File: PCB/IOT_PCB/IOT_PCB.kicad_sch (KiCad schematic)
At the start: 6 parts, among them J1 Screw_Terminal_01x02, J2 Screw_Terminal_01x02, U1 ESP32-S3-WROOM-1, U2 BME280, U3 SCD41-D-R2

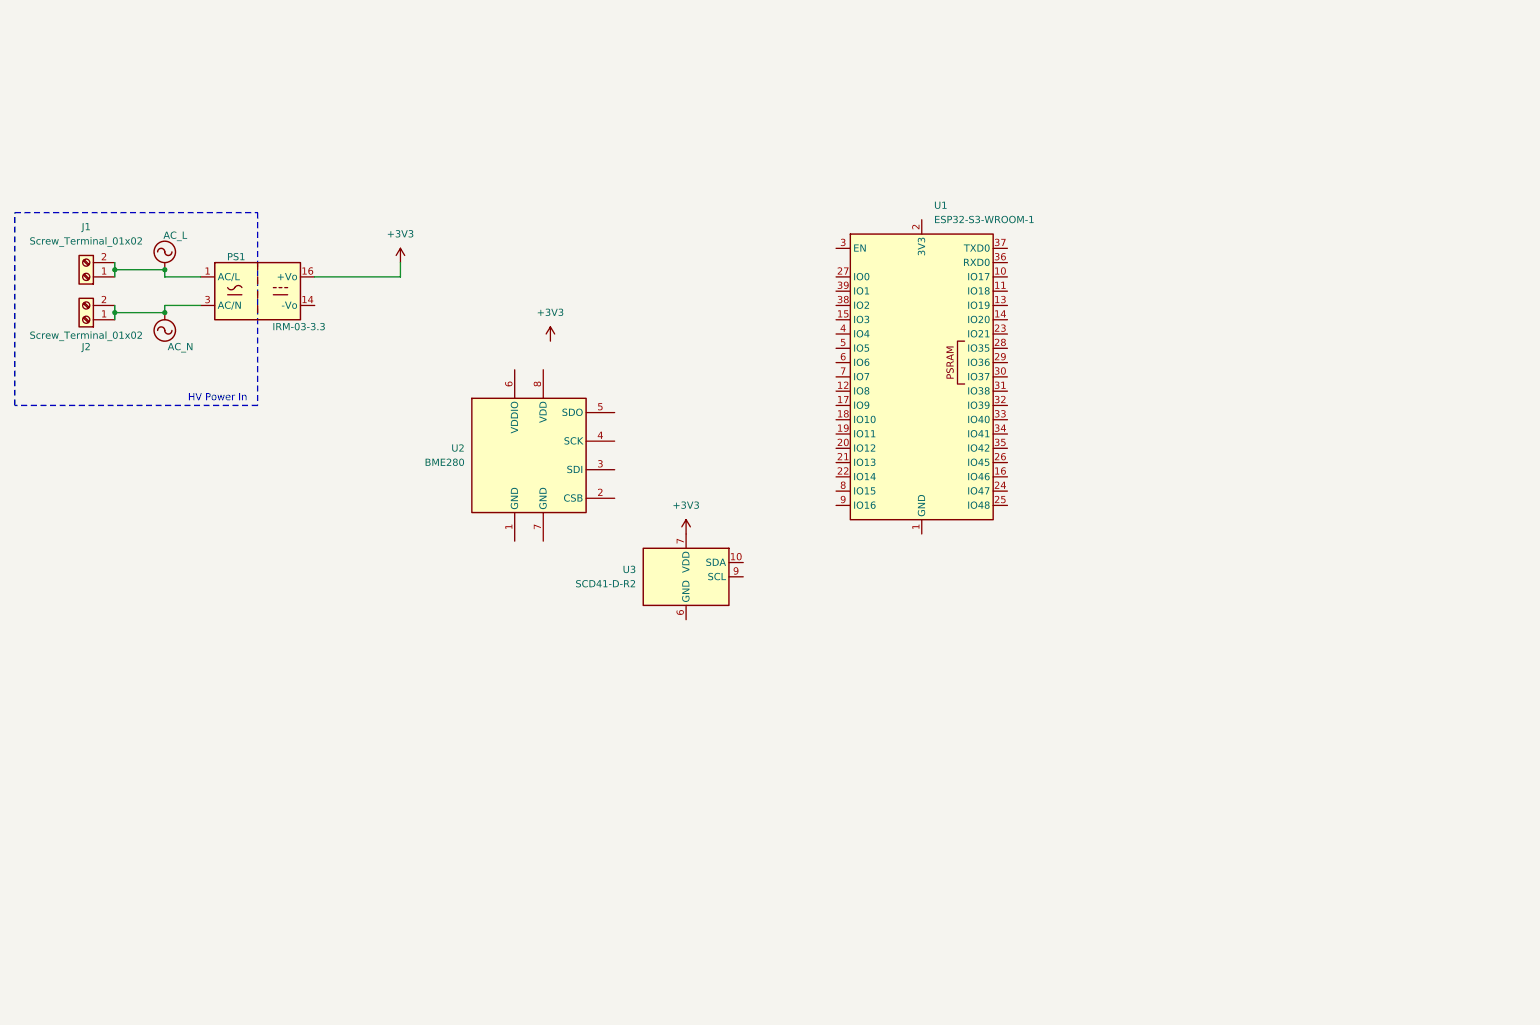
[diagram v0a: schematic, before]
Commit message: Rough component placement and schematic WIP
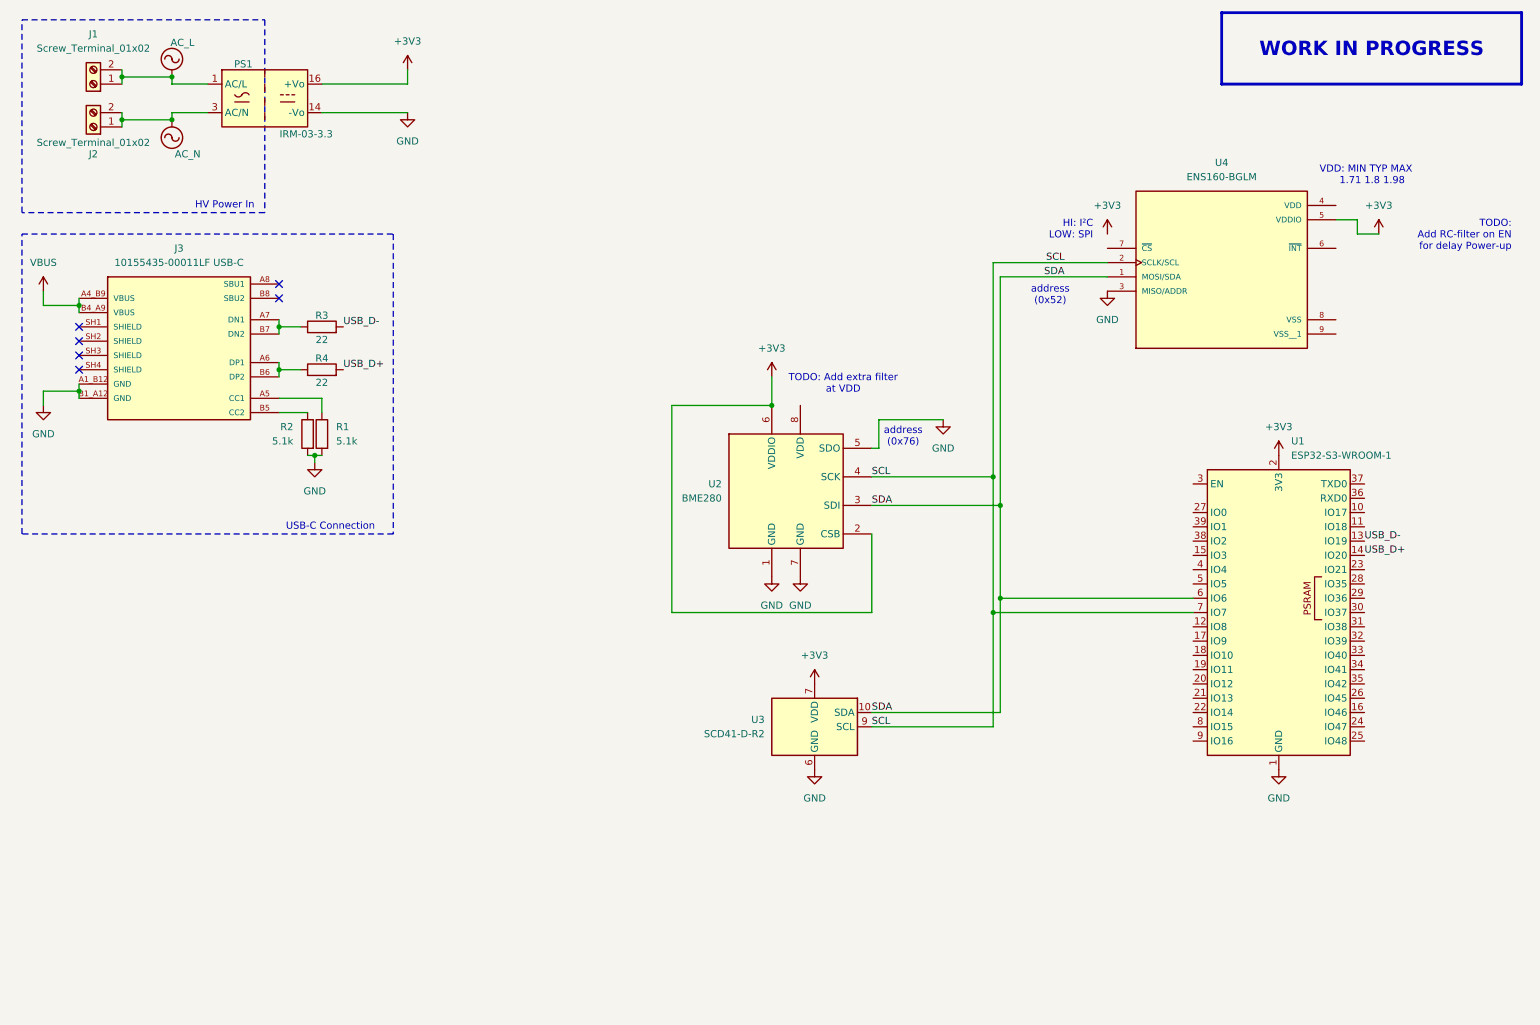
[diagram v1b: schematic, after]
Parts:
- added J3: 10155435-00011LF USB-C, USBC_2 Amphenol 10155435-00011LF:AMPHENOL_10155435-00011LF, symbol 10155435-00011LF:10155435-00011LF
- added R1, R2: 5.1k, Resistor_SMD:R_0805_2012Metric_Pad1.20x1.40mm_HandSolder, symbol Device:R
- added R3, R4: 22, Resistor_SMD:R_0805_2012Metric_Pad1.20x1.40mm_HandSolder, symbol Device:R
- added U4: ENS160-BGLM, ENS160_BGLM:XDCR_ENS160-BGLM, symbol ENS160-BGLM:ENS160-BGLM
- PS1: MANUFACTURER (none) -> Mean Well
- U1: Fält7 ESP32-S3-WROOM-1-N4 -> (none); MANUFACTURER (none) -> Espressif; Mouser No (none) -> 356-ESP32-S3WROOM1N4
- U2: MANUFACTURER (none) -> Bosch
- U3: MANUFACTURER (none) -> Sensirion
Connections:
- net +3V3: now also U1.2 (3V3), U2.2 (CSB), U2.6 (VDDIO), U4.5 (VDDIO)
- net SDA: now reaches U3.10 (SDA)
- net SDA: now also U1.6 (IO6), U2.3 (SDI), U4.1 (MOSI/SDA)
- net GND: now reaches U3.20 (GND), U3.21 (GND), U3.6 (GND)
- net GND: now also PS1.14 (-Vo), U1.1 (GND), U1.40 (GND), U1.41 (GND), U2.1 (GND), U2.5 (SDO), U2.7 (GND), J3.A1_B12 (GND), J3.B1_A12 (GND), R1.2, R2.2, U4.3 (MISO/ADDR)
- net SCL: now reaches U3.9 (SCL)
- net SCL: now also U1.7 (IO7), U2.4 (SCK), U4.2 (SCLK/SCL)
- net USB_D-: now reaches U1.13 (IO19)
- net USB_D-: now also R3.2
- net USB_D+: now reaches U1.14 (IO20)
- net USB_D+: now also R4.2
- new net: J3.A5 (CC1), R1.1
- new net: J3.A6 (DP1), J3.B6 (DP2), R4.1
- new net: J3.A7 (DN1), J3.B7 (DN2), R3.1
- new net: J3.B5 (CC2), R2.1
- new net VBUS: J3.A4_B9 (VBUS), J3.B4_A9 (VBUS)
- no-connect marks 0 -> 6
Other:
- note added: "HI: I²C LOW: SPI"
- note added: "TODO: Add RC-filter on EN for delay Power-up"
- note added: "TODO: Add extra filter at VDD"
- note added: "USB-C Connection"
- note added: "VDD: MIN TYP MAX 1.71 1.8 1.98"
- note added: "address (0x52)"
- note added: "address (0x76)"
- company: (none) -> By: Theofil Eriksson Petrovski
- title: (none) -> Environmental Sensing Module
- moved on the sheet: J1, J2, PS1, U1, U2, U3

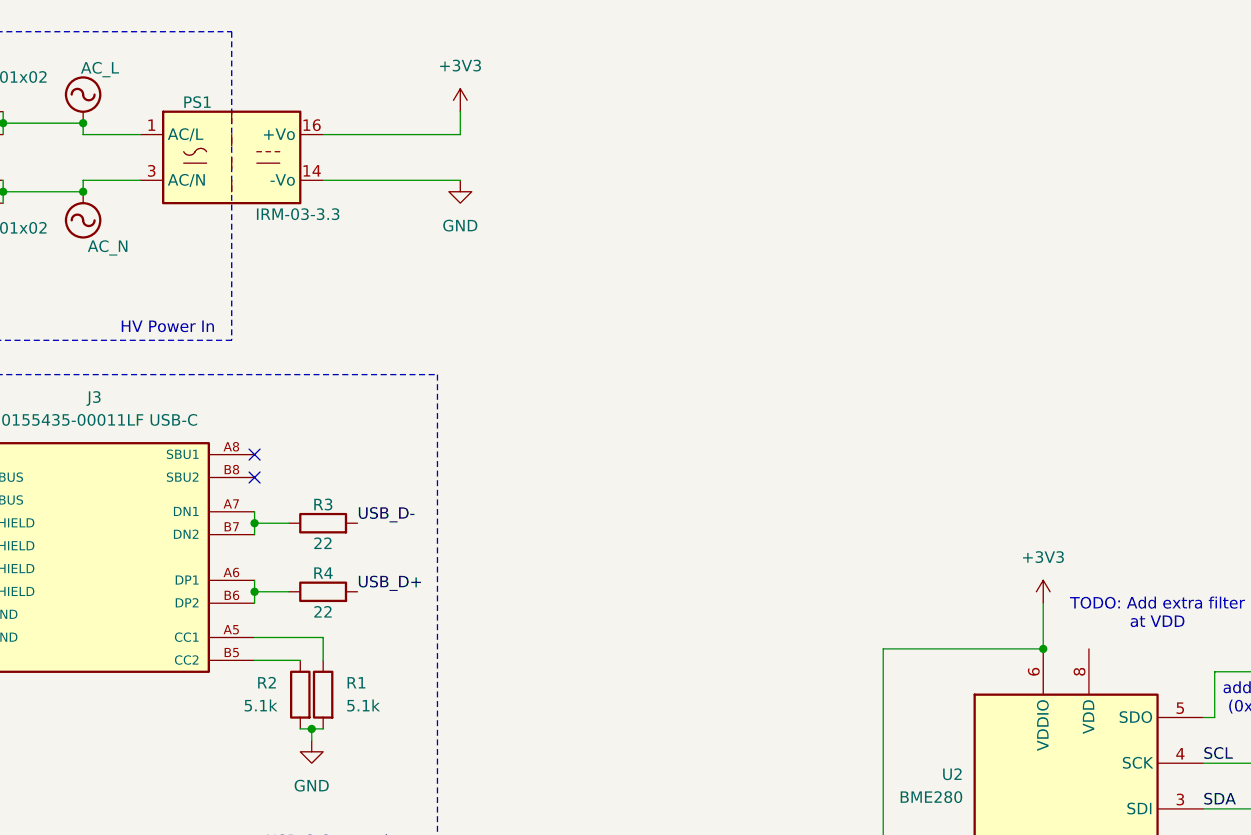
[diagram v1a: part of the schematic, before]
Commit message: Vreg and ESD suppresion
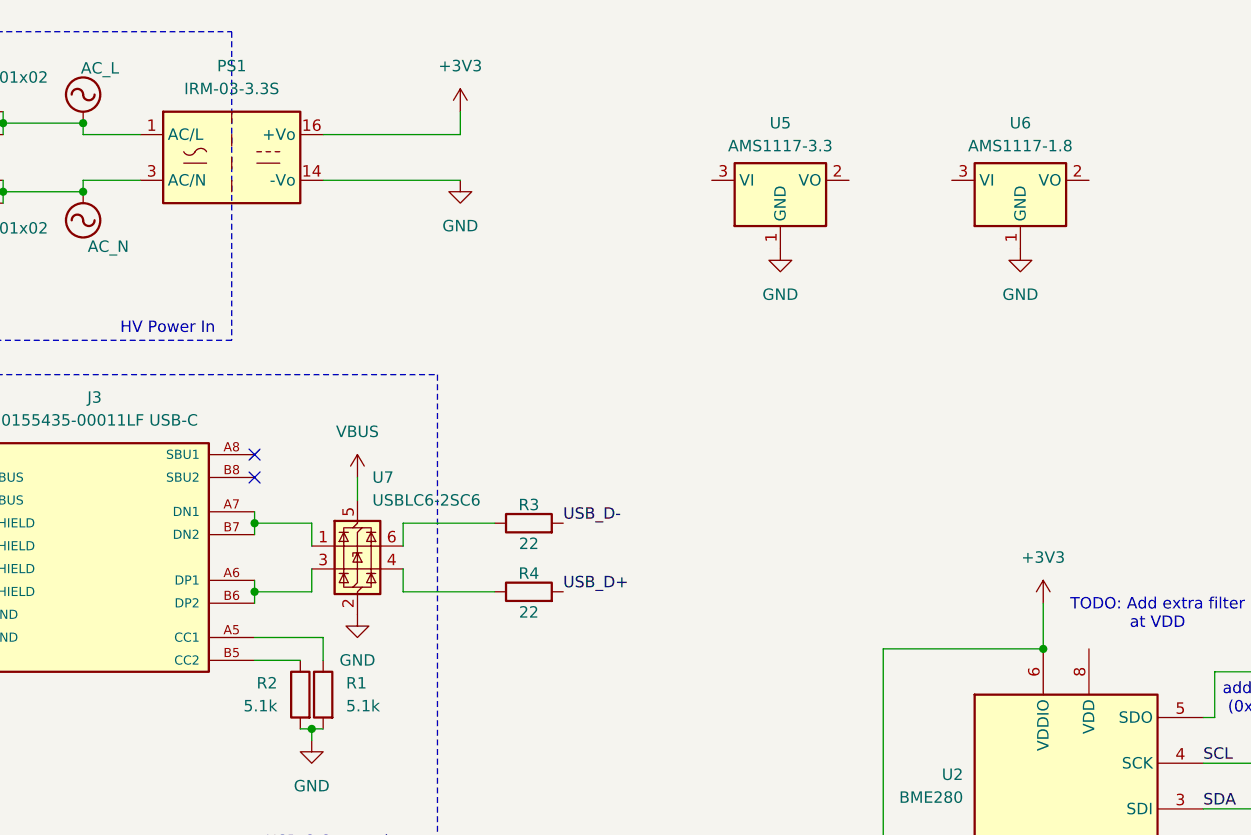
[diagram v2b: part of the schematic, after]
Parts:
- removed PS1: IRM-03-3.3, Converter_ACDC:Converter_ACDC_MeanWell_IRM-03-xx_THT, symbol Converter_ACDC:IRM-03-3.3
- added PS1: IRM-03-3.3S, Converter_ACDC:Converter_ACDC_MeanWell_IRM-03-xx_SMD, symbol Converter_ACDC:IRM-03-3.3S
- added U5: AMS1117-3.3, Package_TO_SOT_SMD:SOT-223-3_TabPin2, symbol Regulator_Linear:AMS1117-3.3
- added U6: AMS1117-1.8, Package_TO_SOT_SMD:SOT-223-3_TabPin2, symbol Regulator_Linear:AMS1117-1.8
- added U7: USBLC6-2SC6, Package_TO_SOT_SMD:SOT-23-6, symbol Power_Protection:USBLC6-2SC6
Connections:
- net +3V3: now also PS1.16 (+Vo)
- net AC_L: now also PS1.1 (AC/L)
- net AC_N: now also PS1.3 (AC/N)
- net GND: now also PS1.14 (-Vo), U5.1 (GND), U6.1 (GND), U7.2 (GND)
- net VBUS: now also U7.5 (VBUS)
- net at J3.A6 (DP1), J3.B6 (DP2): now also U7.3 (I/O2); no longer R4.1
- net at J3.A7 (DN1), J3.B7 (DN2): now also U7.1 (I/O1); no longer R3.1
- new net: R4.1, U7.4 (I/O2)
- new net: R3.1, U7.6 (I/O1)
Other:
- moved on the sheet: R3, R4

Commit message: Shrunk Board
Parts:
- removed U1: ESP32-S3-WROOM-1, RF_Module:ESP32-S3-WROOM-1, symbol RF_Module:ESP32-S3-WROOM-1
- added MH1, MH2, MH3, MH4: MountingHole, MountingHole:MountingHole_3.2mm_M3, symbol Mechanical:MountingHole
- added U1: ESP32-S3-MINI-1, RF_Module:ESP32-S2-MINI-1, symbol RF_Module:ESP32-S3-MINI-1
- J3: Price None -> 8.98 kr
- PS1: MANUFACTURER (none) -> Mean Well; Mouser No (none) -> 709-IRM03-3.3S; Price (none) -> 74.98 kr
- U2: Price 65.52 -> 65.52 kr
- U3: Price 396.75 -> 396.75 kr
- U4: Price 96.60 -> 96.60 kr
- U5, U6: Price (none) -> 12 kr
- U7: Price 3.85 -> 3.85 kr
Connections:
- net +3V3: now also U1.3 (3V3)
- net GND: now also U1.1 (GND), U1.2 (GND), U1.42 (GND), U1.43 (GND), U1.46 (GND), U1.47 (GND), U1.48 (GND), U1.49 (GND), U1.50 (GND), U1.51 (GND), U1.52 (GND), U1.53 (GND), U1.54 (GND), U1.55 (GND), U1.56 (GND), U1.57 (GND), U1.58 (GND), U1.59 (GND), U1.60 (GND), U1.61 (GND), U1.62 (GND), U1.63 (GND), U1.64 (GND), U1.65 (GND)
- net SCL: now also U1.11 (IO7)
- net SDA: now also U1.10 (IO6)
- net USB_D+: now also U1.24 (IO20)
- net USB_D-: now also U1.23 (IO19)
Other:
- note added: "1v8 or 3v3 1ma"
- note added: "3v3 or 5v 200ma"
- note added: "CO2"
- note added: "Main microcontroller w/ Integrated WIFI/Bluetooth"
- note added: "TODO: Add capacitors Add filters Add control for different voltage supplies Add extra outputs Maybe add fan output? Add fuses"
- note added: "TVOC sensor"
- note added: "Temperature Humidity Pressure"
